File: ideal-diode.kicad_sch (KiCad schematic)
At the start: 4 parts, among them Q5 SI7613DN-T1-GE3, U10 LTC4412IS6

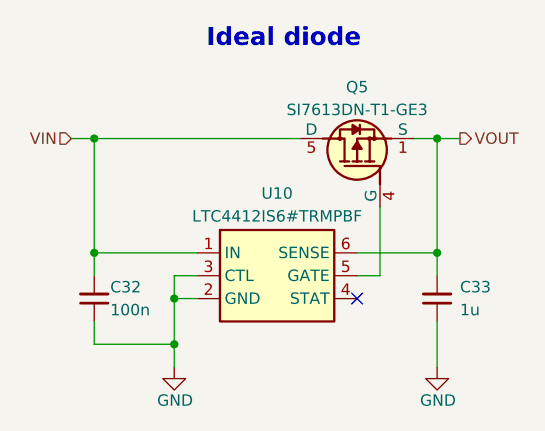
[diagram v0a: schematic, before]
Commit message: [#79262] Finish power section schematic
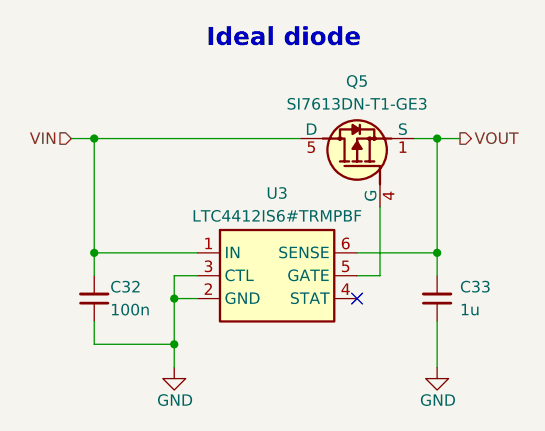
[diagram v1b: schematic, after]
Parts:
- renumbered U10 to U3
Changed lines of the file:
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@@
 		(instances
 			(project "oculink-to-pcie-adapter"
-				(path "/44c3be85-0a18-4d93-a9a5-650ee09b6032/a873a5d6-7a36-44dd-8353-37b193324816"
-					(reference "C36")
-					(unit 1)
-				)
-				(path "/44c3be85-0a18-4d93-a9a5-650ee09b6032/abe40e29-8440-4917-abf7-be311a7a4dc1"
+				(path "/44c3be85-0a18-4d93-a9a5-650ee09b6032/38f25804-42b6-4fac-b87c-d8c0064ff23c/2c9dd899-fea0-4553-a2ec-dc9a1ce7e79c"
+					(reference "C34")
+					(unit 1)
+				)
+				(path "/44c3be85-0a18-4d93-a9a5-650ee09b6032/38f25804-42b6-4fac-b87c-d8c0064ff23c/6d13e59e-b137-42bb-8790-0fd656b28a3d"
 					(reference "C32")
 					(unit 1)
@@
 	)
 	(symbol
-		(lib_name "LTC4412IS6_1")
 		(lib_id "antmicroPMICORControllersIdealDiodes:LTC4412IS6")
 		(at 196.85 152.4 0)
@@
 		(on_board yes)
 		(dnp no)
-		(property "Reference" "U10"
+		(property "Reference" "U3"
 			(at 205.74 145.796 0)
 			(effects
@@
 		(instances
 			(project "oculink-to-pcie-adapter"
-				(path "/44c3be85-0a18-4d93-a9a5-650ee09b6032/a873a5d6-7a36-44dd-8353-37b193324816"
-					(reference "U12")
-					(unit 1)
-				)
-				(path "/44c3be85-0a18-4d93-a9a5-650ee09b6032/abe40e29-8440-4917-abf7-be311a7a4dc1"
-					(reference "U10")
+				(path "/44c3be85-0a18-4d93-a9a5-650ee09b6032/38f25804-42b6-4fac-b87c-d8c0064ff23c/2c9dd899-fea0-4553-a2ec-dc9a1ce7e79c"
+					(reference "U4")
+					(unit 1)
+				)
+				(path "/44c3be85-0a18-4d93-a9a5-650ee09b6032/38f25804-42b6-4fac-b87c-d8c0064ff23c/6d13e59e-b137-42bb-8790-0fd656b28a3d"
+					(reference "U3")
 					(unit 1)
 				)
@@
 		(fields_autoplaced yes)
 		(property "Reference" "Q5"
-			(at 214.63 133.9764 90)
-			(effects
-				(font
-					(size 1.27 1.27)
+			(at 214.63 133.35 90)
+			(effects
+				(font
+					(size 1.27 1.27)
+					(thickness 0.15)
 				)
 			)
 		)
 		(property "Value" "SI7613DN-T1-GE3"
-			(at 214.63 136.5067 90)
-			(effects
-				(font
-					(size 1.27 1.27)
-					(thickness 0.15)
-				)
+			(at 214.63 132.08 0)
+			(effects
+				(font
+					(size 1.27 1.27)
+					(thickness 0.15)
+				)
+				(justify left bottom)
+				(hide yes)
 			)
 		)
@@
 			)
 		)
-		(property "Description" ""
-			(at 217.17 147.32 0)
-			(effects
-				(font
-					(size 1.27 1.27)
-				)
+		(property "Description" "Power MOSFET, P Channel, 20 V, 35 A, 0.0072 ohm, PowerPAK 1212, Surface Mount"
+			(at 231.394 90.932 0)
+			(effects
+				(font
+					(size 1.27 1.27)
+				)
+				(hide yes)
 			)
 		)
 		(property "MPN" "SI7613DN-T1-GE3"
-			(at 222.25 132.08 0)
-			(effects
-				(font
-					(size 1.27 1.27)
-					(thickness 0.15)
-				)
-				(justify left bottom)
-				(hide yes)
+			(at 214.63 135.89 90)
+			(effects
+				(font
+					(size 1.27 1.27)
+					(thickness 0.15)
+				)
 			)
 		)
@@
 			)
 		)
+		(pin "3"
+		)
 		(pin "1"
 		)
+		(pin "4"
+		)
 		(pin "2"
-		)
-		(pin "3"
-		)
-		(pin "4"
 		)
 		(pin "5"
@@
 		(instances
 			(project "oculink-to-pcie-adapter"
-				(path "/44c3be85-0a18-4d93-a9a5-650ee09b6032/a873a5d6-7a36-44dd-8353-37b193324816"
-					(reference "Q7")
-					(unit 1)
-				)
-				(path "/44c3be85-0a18-4d93-a9a5-650ee09b6032/abe40e29-8440-4917-abf7-be311a7a4dc1"
+				(path "/44c3be85-0a18-4d93-a9a5-650ee09b6032/38f25804-42b6-4fac-b87c-d8c0064ff23c/2c9dd899-fea0-4553-a2ec-dc9a1ce7e79c"
+					(reference "Q6")
+					(unit 1)
+				)
+				(path "/44c3be85-0a18-4d93-a9a5-650ee09b6032/38f25804-42b6-4fac-b87c-d8c0064ff23c/6d13e59e-b137-42bb-8790-0fd656b28a3d"
 					(reference "Q5")
 					(unit 1)
@@
 		(dnp no)
 		(fields_autoplaced yes)
-		(property "Reference" "#PWR081"
+		(property "Reference" "#PWR080"
 			(at 194.31 171.45 0)
 			(effects
@@
 		(instances
 			(project "oculink-to-pcie-adapter"
-				(path "/44c3be85-0a18-4d93-a9a5-650ee09b6032/a873a5d6-7a36-44dd-8353-37b193324816"
-					(reference "#PWR086")
-					(unit 1)
-				)
-				(path "/44c3be85-0a18-4d93-a9a5-650ee09b6032/abe40e29-8440-4917-abf7-be311a7a4dc1"
-					(reference "#PWR081")
+				(path "/44c3be85-0a18-4d93-a9a5-650ee09b6032/38f25804-42b6-4fac-b87c-d8c0064ff23c/2c9dd899-fea0-4553-a2ec-dc9a1ce7e79c"
+					(reference "#PWR082")
+					(unit 1)
+				)
+				(path "/44c3be85-0a18-4d93-a9a5-650ee09b6032/38f25804-42b6-4fac-b87c-d8c0064ff23c/6d13e59e-b137-42bb-8790-0fd656b28a3d"
+					(reference "#PWR080")
 					(unit 1)
 				)
@@
 	)
 	(symbol
-		(lib_name "C_1u_25V_0603_1")
 		(lib_id "antmicroCapacitors0603:C_1u_25V_0603")
 		(at 223.52 160.02 90)
@@
 		(instances
 			(project "oculink-to-pcie-adapter"
-				(path "/44c3be85-0a18-4d93-a9a5-650ee09b6032/a873a5d6-7a36-44dd-8353-37b193324816"
-					(reference "C37")
-					(unit 1)
-				)
-				(path "/44c3be85-0a18-4d93-a9a5-650ee09b6032/abe40e29-8440-4917-abf7-be311a7a4dc1"
+				(path "/44c3be85-0a18-4d93-a9a5-650ee09b6032/38f25804-42b6-4fac-b87c-d8c0064ff23c/2c9dd899-fea0-4553-a2ec-dc9a1ce7e79c"
+					(reference "C35")
+					(unit 1)
+				)
+				(path "/44c3be85-0a18-4d93-a9a5-650ee09b6032/38f25804-42b6-4fac-b87c-d8c0064ff23c/6d13e59e-b137-42bb-8790-0fd656b28a3d"
 					(reference "C33")
 					(unit 1)
@@
 		(dnp no)
 		(fields_autoplaced yes)
-		(property "Reference" "#PWR082"
+		(property "Reference" "#PWR081"
 			(at 223.52 171.45 0)
 			(effects
@@
 		(instances
 			(project "oculink-to-pcie-adapter"
-				(path "/44c3be85-0a18-4d93-a9a5-650ee09b6032/a873a5d6-7a36-44dd-8353-37b193324816"
-					(reference "#PWR087")
-					(unit 1)
-				)
-				(path "/44c3be85-0a18-4d93-a9a5-650ee09b6032/abe40e29-8440-4917-abf7-be311a7a4dc1"
-					(reference "#PWR082")
-					(unit 1)
-				)
+				(path "/44c3be85-0a18-4d93-a9a5-650ee09b6032/38f25804-42b6-4fac-b87c-d8c0064ff23c/2c9dd899-fea0-4553-a2ec-dc9a1ce7e79c"
+					(reference "#PWR084")
+					(unit 1)
+				)
+				(path "/44c3be85-0a18-4d93-a9a5-650ee09b6032/38f25804-42b6-4fac-b87c-d8c0064ff23c/6d13e59e-b137-42bb-8790-0fd656b28a3d"
+					(reference "#PWR081")
+					(unit 1)
+				)

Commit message: [#79262] BOM consolidation
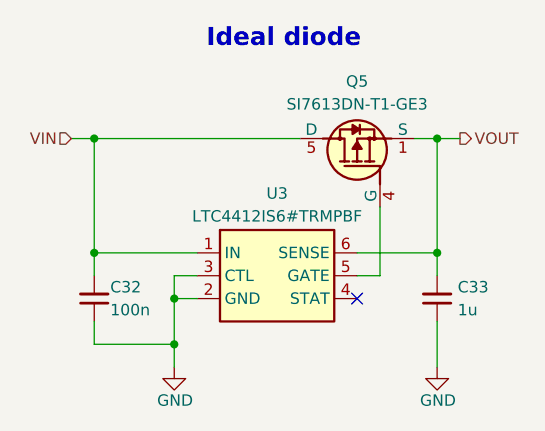
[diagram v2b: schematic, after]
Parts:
- removed C33: C_1u_25V_0603, antmicro-footprints:C_0603_1608Metric, symbol antmicroCapacitors0603:C_1u_25V_0603
- added C33: C_1u_25V_0402, antmicro-footprints:C_0402_1005Metric, symbol antmicroCapacitors0402:C_1u_25V_0402
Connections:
- net GND: now also C33.1
- net VOUT: now also C33.2
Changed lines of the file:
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@@
 	)
 	(symbol
-		(lib_id "antmicroCapacitors0603:C_1u_25V_0603")
+		(lib_id "antmicroCapacitors0402:C_1u_25V_0402")
 		(at 223.52 160.02 90)
 		(unit 1)
@@
 		(on_board yes)
 		(dnp no)
-		(fields_autoplaced yes)
 		(property "Reference" "C33"
-			(at 226.06 156.2036 90)
+			(at 225.806 156.21 90)
 			(effects
 				(font
@@
 			)
 		)
-		(property "Value" "C_1u_25V_0603"
+		(property "Value" "C_1u_25V_0402"
 			(at 233.68 139.7 0)
 			(effects
@@
 			)
 		)
-		(property "Footprint" "antmicro-footprints:C_0603_1608Metric"
+		(property "Footprint" "antmicro-footprints:C_0402_1005Metric"
 			(at 236.22 139.7 0)
 			(effects
@@
 			)
 		)
-		(property "Datasheet" "https://product.samsungsem.com/mlcc/CL10A105KA8NNN.do"
+		(property "Datasheet" "https://www.murata.com/products/productdetail?partno=GRM155R61E105KE11%23"
 			(at 238.76 139.7 0)
 			(effects
@@
 			)
 		)
-		(property "Description" "SMD Multilayer Ceramic Capacitor, 1 µF, 25 V, 0603 [1608 Metric], ± 10%, X5R, CL"
+		(property "Description" "SMD Multilayer Ceramic Capacitor, 1 µF, 25 V, 0402 [1005 Metric], ± 10%, X5R, GRM Series"
 			(at 223.52 160.02 0)
 			(effects
@@
 			)
 		)
-		(property "MPN" "CL10A105KA8NNNC"
+		(property "MPN" "GRM155R61E105KE11J"
 			(at 241.3 139.7 0)
 			(effects
@@
 			)
 		)
-		(property "Manufacturer" "Samsung Electro-Mechanics"
+		(property "Manufacturer" "Murata"
 			(at 243.84 139.7 0)
 			(effects
@@
 		)
 		(property "Val" "1u"
-			(at 226.06 158.7436 90)
+			(at 225.806 158.75 90)
 			(effects
 				(font
@@
 			)
 		)
-		(property "Dielectric" ""
+		(property "Dielectric" "X5R"
 			(at 254 139.7 0)
 			(effects
@@
 			)
 		)
+		(pin "2"
+		)
 		(pin "1"
 		)
-		(pin "2"
-		)
 		(instances

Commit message: [#79262] Further BOM consolidation
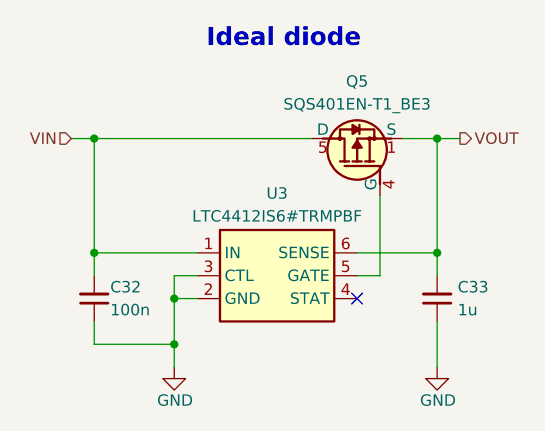
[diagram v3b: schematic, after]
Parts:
- removed Q5: SI7613DN-T1-GE3, antmicro-footprints:Vishay_PowerPAK_1212-8_Single, symbol antmicroTransistorsFETsMOSFETsSingle:SI7613DN-T1-GE3
- added Q5: SQS401EN-T1_BE3, antmicro-footprints:Vishay_PowerPAK_1212-8_Single, symbol antmicroTransistorsFETsMOSFETsSingle:SQS401EN-T1_BE3
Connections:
- net VIN: now also Q5.5 (D)
- net VOUT: now also Q5.1 (S), Q5.2 (S), Q5.3 (S)
- net at U3.5 (GATE): now also Q5.4 (G)
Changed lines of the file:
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@@
 	(wire
 		(pts
-			(xy 217.17 154.94) (xy 217.17 147.32)
+			(xy 217.17 146.05) (xy 217.17 154.94)
 		)
 		(stroke
@@
 	(wire
 		(pts
+			(xy 219.71 139.7) (xy 223.52 139.7)
+		)
+		(stroke
+			(width 0)
+			(type default)
+		)
+	)
+	(wire
+		(pts
 			(xy 214.63 154.94) (xy 217.17 154.94)
 		)
@@
 	(wire
 		(pts
-			(xy 220.98 139.7) (xy 223.52 139.7)
-		)
-		(stroke
-			(width 0)
-			(type default)
-		)
-	)
-	(wire
-		(pts
 			(xy 214.63 152.4) (xy 223.52 152.4)
 		)
@@
 	(wire
 		(pts
-			(xy 185.42 139.7) (xy 208.28 139.7)
+			(xy 185.42 139.7) (xy 209.55 139.7)
 		)
 		(stroke
@@
 				(path "/44c3be85-0a18-4d93-a9a5-650ee09b6032/38f25804-42b6-4fac-b87c-d8c0064ff23c/6d13e59e-b137-42bb-8790-0fd656b28a3d"
 					(reference "U3")
-					(unit 1)
-				)
-			)
-		)
-	)
-	(symbol
-		(lib_id "antmicroTransistorsFETsMOSFETsSingle:SI7613DN-T1-GE3")
-		(at 217.17 147.32 90)
-		(unit 1)
-		(exclude_from_sim no)
-		(in_bom yes)
-		(on_board yes)
-		(dnp no)
-		(fields_autoplaced yes)
-		(property "Reference" "Q5"
-			(at 214.63 133.35 90)
-			(effects
-				(font
-					(size 1.27 1.27)
-					(thickness 0.15)
-				)
-			)
-		)
-		(property "Value" "SI7613DN-T1-GE3"
-			(at 214.63 132.08 0)
-			(effects
-				(font
-					(size 1.27 1.27)
-					(thickness 0.15)
-				)
-				(justify left bottom)
-				(hide yes)
-			)
-		)
-		(property "Footprint" "antmicro-footprints:Vishay_PowerPAK_1212-8_Single"
-			(at 215.9 132.08 0)
-			(effects
-				(font
-					(size 1.27 1.27)
-					(thickness 0.15)
-				)
-				(justify left bottom)
-				(hide yes)
-			)
-		)
-		(property "Datasheet" "https://www.vishay.com/docs/64809/si7613dn.pdf"
-			(at 218.44 132.08 0)
-			(effects
-				(font
-					(size 1.27 1.27)
-					(thickness 0.15)
-				)
-				(justify left bottom)
-				(hide yes)
-			)
-		)
-		(property "Description" "Power MOSFET, P Channel, 20 V, 35 A, 0.0072 ohm, PowerPAK 1212, Surface Mount"
-			(at 231.394 90.932 0)
-			(effects
-				(font
-					(size 1.27 1.27)
-				)
-				(hide yes)
-			)
-		)
-		(property "MPN" "SI7613DN-T1-GE3"
-			(at 214.63 135.89 90)
-			(effects
-				(font
-					(size 1.27 1.27)
-					(thickness 0.15)
-				)
-			)
-		)
-		(property "Manufacturer" "Vishay"
-			(at 224.79 132.08 0)
-			(effects
-				(font
-					(size 1.27 1.27)
-					(thickness 0.15)
-				)
-				(justify left bottom)
-				(hide yes)
-			)
-		)
-		(property "Author" "Antmicro"
-			(at 227.33 132.08 0)
-			(effects
-				(font
-					(size 1.27 1.27)
-					(thickness 0.15)
-				)
-				(justify left bottom)
-				(hide yes)
-			)
-		)
-		(property "License" "Apache-2.0"
-			(at 229.87 132.08 0)
-			(effects
-				(font
-					(size 1.27 1.27)
-					(thickness 0.15)
-				)
-				(justify left bottom)
-				(hide yes)
-			)
-		)
-		(pin "3"
-		)
-		(pin "1"
-		)
-		(pin "4"
-		)
-		(pin "2"
-		)
-		(pin "5"
-		)
-		(instances
-			(project "oculink-to-pcie-adapter"
-				(path "/44c3be85-0a18-4d93-a9a5-650ee09b6032/38f25804-42b6-4fac-b87c-d8c0064ff23c/2c9dd899-fea0-4553-a2ec-dc9a1ce7e79c"
-					(reference "Q6")
-					(unit 1)
-				)
-				(path "/44c3be85-0a18-4d93-a9a5-650ee09b6032/38f25804-42b6-4fac-b87c-d8c0064ff23c/6d13e59e-b137-42bb-8790-0fd656b28a3d"
-					(reference "Q5")
 					(unit 1)
 				)
@@
 					(unit 1)
 				)
+			)
+		)
+	)
+	(symbol
+		(lib_id "antmicroTransistorsFETsMOSFETsSingle:SQS401EN-T1_BE3")
+		(at 217.17 146.05 90)
+		(unit 1)
+		(exclude_from_sim no)
+		(in_bom yes)
+		(on_board yes)
+		(dnp no)
+		(property "Reference" "Q5"
+			(at 214.63 133.35 90)
+			(effects
+				(font
+					(size 1.27 1.27)
+					(thickness 0.15)
+				)
+			)
+		)
+		(property "Value" "SQS401EN-T1_BE3"
+			(at 227.33 130.81 0)
+			(effects
+				(font
+					(size 1.27 1.27)
+					(thickness 0.15)
+				)
+				(justify left bottom)
+				(hide yes)
+			)
+		)
+		(property "Footprint" "antmicro-footprints:Vishay_PowerPAK_1212-8_Single"
+			(at 229.87 130.81 0)
+			(effects
+				(font
+					(size 1.27 1.27)
+					(thickness 0.15)
+				)
+				(justify left bottom)
+				(hide yes)
+			)
+		)
+		(property "Datasheet" "https://www.vishay.com/docs/65529/sqs401en.pdf"
+			(at 232.41 130.81 0)
+			(effects
+				(font
+					(size 1.27 1.27)
+					(thickness 0.15)
+				)
+				(justify left bottom)
+				(hide yes)
+			)
+		)
+		(property "Description" "MOSFET, P Channel, 40 V, 16A, 0.047 ohm, PowerPAK 1212-8, Surface Mount"
+			(at 217.17 146.05 0)
+			(effects
+				(font
+					(size 1.27 1.27)
+				)
+				(hide yes)
+			)
+		)
+		(property "MPN" "SQS401EN-T1_BE3"
+			(at 214.63 135.89 90)
+			(effects
+				(font
+					(size 1.27 1.27)
+					(thickness 0.15)
+				)
+			)
+		)
+		(property "Manufacturer" "Vishay"
+			(at 234.95 130.81 0)
+			(effects
+				(font
+					(size 1.27 1.27)
+					(thickness 0.15)
+				)
+				(justify left bottom)
+				(hide yes)
+			)
+		)
+		(property "Author" "Antmicro"
+			(at 237.49 130.81 0)
+			(effects
+				(font
+					(size 1.27 1.27)
+					(thickness 0.15)
+				)
+				(justify left bottom)
+				(hide yes)
+			)
+		)
+		(property "License" "Apache-2.0"
+			(at 240.03 130.81 0)
+			(effects
+				(font
+					(size 1.27 1.27)
+					(thickness 0.15)
+				)
+				(justify left bottom)
+				(hide yes)
+			)
+		)
+		(pin "4"
+		)
+		(pin "1"
+		)
+		(pin "3"
+		)
+		(pin "5"
+		)
+		(pin "2"
+		)
+		(instances
+			(project "oculink-to-pcie-adapter"
+				(path "/44c3be85-0a18-4d93-a9a5-650ee09b6032/38f25804-42b6-4fac-b87c-d8c0064ff23c/2c9dd899-fea0-4553-a2ec-dc9a1ce7e79c"
+					(reference "Q1")
+					(unit 1)
+				)
+				(path "/44c3be85-0a18-4d93-a9a5-650ee09b6032/38f25804-42b6-4fac-b87c-d8c0064ff23c/6d13e59e-b137-42bb-8790-0fd656b28a3d"
+					(reference "Q5")
+					(unit 1)
+				)
